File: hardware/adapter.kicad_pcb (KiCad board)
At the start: 2 copper layers, 51 parts

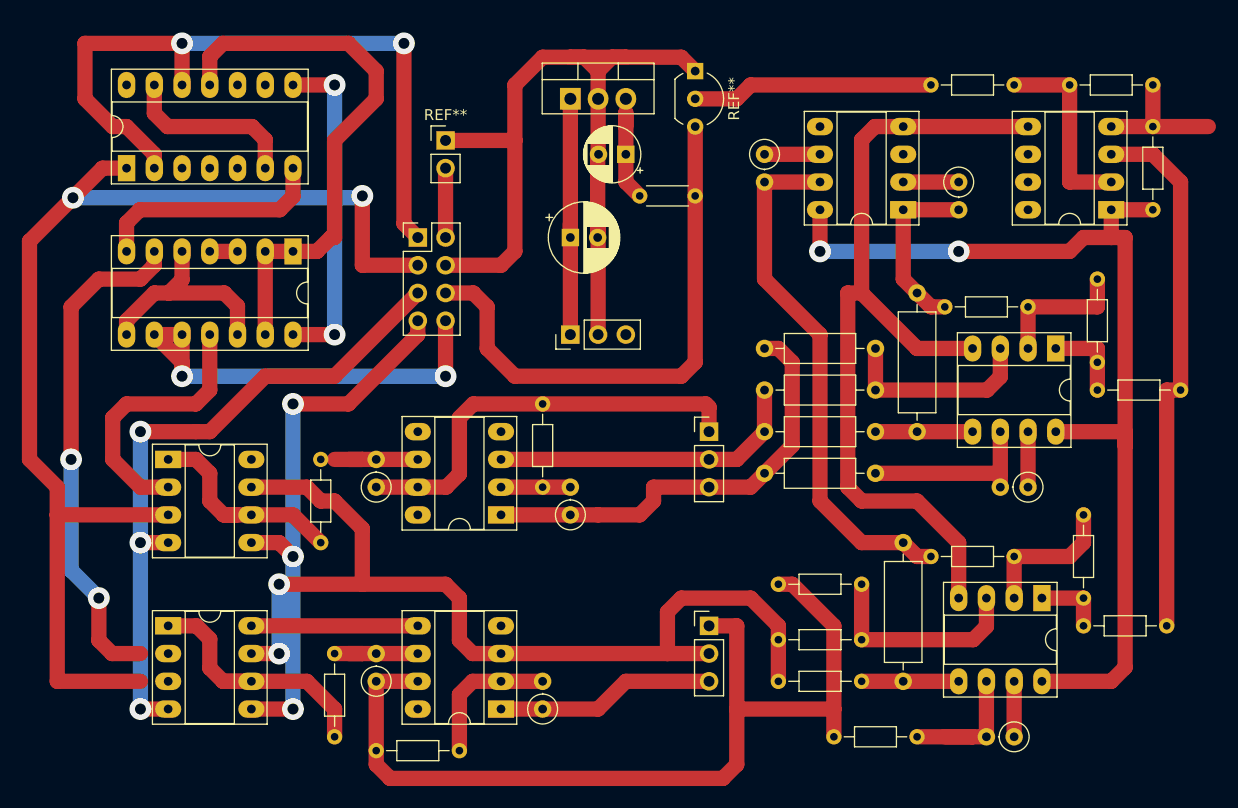
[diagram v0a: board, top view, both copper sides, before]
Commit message: Full hardware plate schema
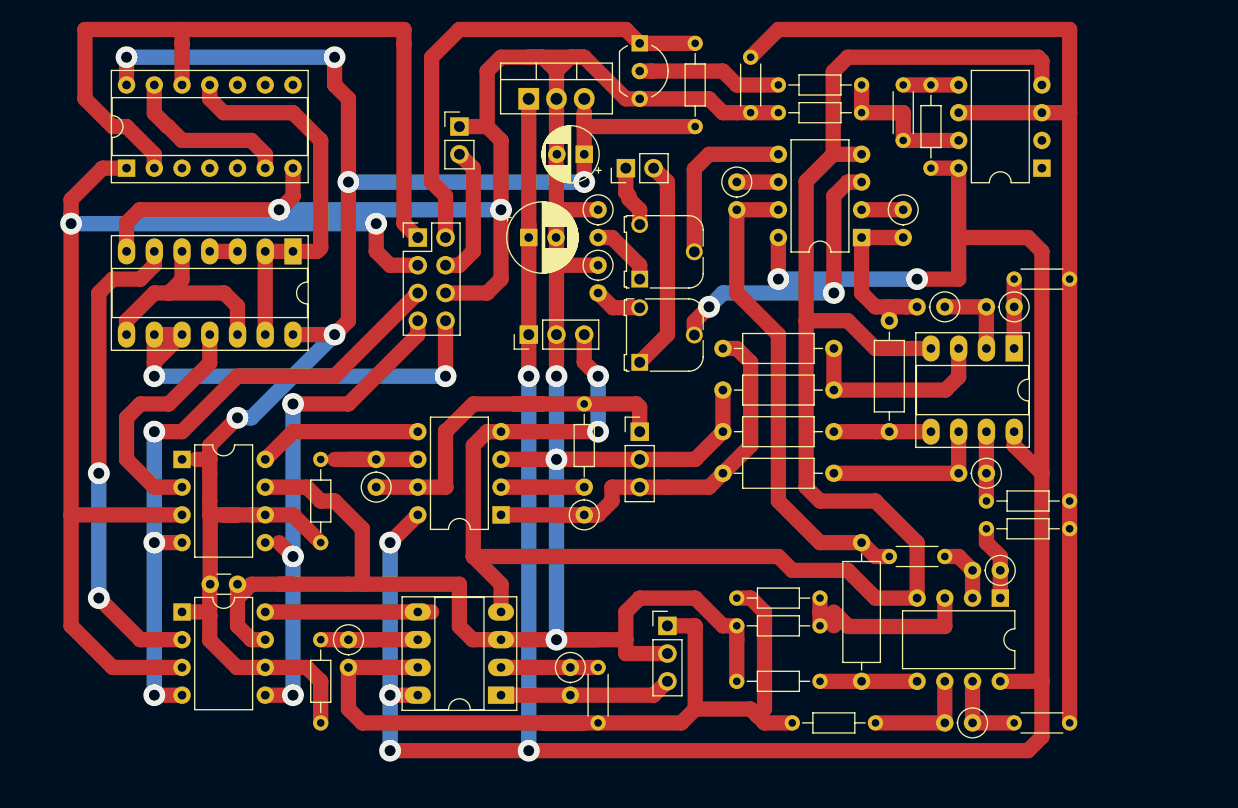
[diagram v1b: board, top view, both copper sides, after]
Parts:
- removed the REF** at (111.8, 27.9)
- removed the REF** at (118.1, 67.3)
- removed the REF** at (118.1, 49.5)
- removed the REF** at (68.6, 67.3)
- removed the REF** at (87.6, 78.7)
- removed the REF** at (151.1, 17.8)
- removed the REF** at (158.8, 21.6)
- removed the REF** at (153.7, 45.7)
- removed the REF** at (123.2, 53.3)
- removed the REF** at (123.2, 49.5)
- removed the REF** at (123.2, 45.7)
- removed the REF** at (154.9, 29.2)
- removed the REF** at (138.4, 61.0)
- removed the REF** at (152.4, 57.1)
- removed the REF** at (148.6, 64.8)
- removed the REF** at (139.7, 38.1)
- removed the REF** at (137.2, 36.8)
- removed the REF** at (153.7, 35.6)
- removed the REF** at (123.2, 24.1)
- removed the REF** at (141.0, 26.7)
- removed the REF** at (149.9, 41.9)
- removed the REF** at (135.9, 29.2)
- removed the REF** at (99.1, 57.1)
- removed the REF** at (68.6, 52.1)
- removed the REF** at (64.8, 25.4)
- removed the REF** at (105.4, 57.1)
- removed the REF** at (102.9, 74.9)
- added REF**: DIP-8_W7.62mm, Package_DIP:DIP-8_W7.62mm, F.Cu at (69.8, 52.1)
- added REF**: DIP-14_W7.62mm_Socket, Package_DIP:DIP-14_W7.62mm_Socket, F.Cu at (64.8, 25.4)
- added REF**: DIP-8_W7.62mm, Package_DIP:DIP-8_W7.62mm, F.Cu at (69.8, 66.0)
- added REF**: R_Axial_DIN0207_L6.3mm_D2.5mm_P2.54mm_Vertical, Resistor_THT:R_Axial_DIN0207_L6.3mm_D2.5mm_P2.54mm_Vertical, F.Cu at (108.0, 34.3)
- added REF**: R_Axial_DIN0207_L6.3mm_D2.5mm_P2.54mm_Vertical, Resistor_THT:R_Axial_DIN0207_L6.3mm_D2.5mm_P2.54mm_Vertical, F.Cu at (108.0, 29.2)
- added REF**: R_Axial_DIN0204_L3.6mm_D1.6mm_P7.62mm_Horizontal, Resistor_THT:R_Axial_DIN0204_L3.6mm_D1.6mm_P7.62mm_Horizontal, F.Cu at (116.8, 21.6)
- added REF**: PinHeader_1x02_P2.54mm_Vertical, Connector_PinHeader_2.54mm:PinHeader_1x02_P2.54mm_Vertical, F.Cu at (110.5, 25.4)
- added REF**: DIP-8_W7.62mm, Package_DIP:DIP-8_W7.62mm, F.Cu at (132.1, 31.8)
- added REF**: Potentiometer_Runtron_RM-065_Vertical, Potentiometer_THT:Potentiometer_Runtron_RM-065_Vertical, F.Cu at (111.8, 35.6)
- added REF**: R_Axial_DIN0204_L3.6mm_D1.6mm_P5.08mm_Horizontal, Resistor_THT:R_Axial_DIN0204_L3.6mm_D1.6mm_P5.08mm_Horizontal, F.Cu at (146.1, 76.2)
- added REF**: R_Axial_DIN0204_L3.6mm_D1.6mm_P7.62mm_Horizontal, Resistor_THT:R_Axial_DIN0204_L3.6mm_D1.6mm_P7.62mm_Horizontal, F.Cu at (143.5, 55.9)
- added REF**: DIP-8_W7.62mm, Package_DIP:DIP-8_W7.62mm, F.Cu at (148.6, 25.4)
- added REF**: DIP-8_W7.62mm, Package_DIP:DIP-8_W7.62mm, F.Cu at (144.8, 64.8)
- added REF**: DIP-8_W7.62mm, Package_DIP:DIP-8_W7.62mm, F.Cu at (99.1, 57.1)
- added REF**: R_Axial_DIN0204_L3.6mm_D1.6mm_P7.62mm_Horizontal, Resistor_THT:R_Axial_DIN0204_L3.6mm_D1.6mm_P7.62mm_Horizontal, F.Cu at (124.5, 17.8)
- added REF**: R_Axial_DIN0204_L3.6mm_D1.6mm_P5.08mm_Horizontal, Resistor_THT:R_Axial_DIN0204_L3.6mm_D1.6mm_P5.08mm_Horizontal, F.Cu at (135.9, 22.9)
- added REF**: R_Axial_DIN0207_L6.3mm_D2.5mm_P10.16mm_Horizontal, Resistor_THT:R_Axial_DIN0207_L6.3mm_D2.5mm_P10.16mm_Horizontal, F.Cu at (134.6, 49.5)
- added REF**: R_Axial_DIN0204_L3.6mm_D1.6mm_P5.08mm_Horizontal, Resistor_THT:R_Axial_DIN0204_L3.6mm_D1.6mm_P5.08mm_Horizontal, F.Cu at (146.1, 35.6)
- added REF**: Potentiometer_Runtron_RM-065_Vertical, Potentiometer_THT:Potentiometer_Runtron_RM-065_Vertical, F.Cu at (111.8, 43.2)
- added REF**: R_Axial_DIN0207_L6.3mm_D2.5mm_P2.54mm_Vertical, Resistor_THT:R_Axial_DIN0207_L6.3mm_D2.5mm_P2.54mm_Vertical, F.Cu at (144.8, 62.2)
- added REF**: R_Axial_DIN0207_L6.3mm_D2.5mm_P2.54mm_Vertical, Resistor_THT:R_Axial_DIN0207_L6.3mm_D2.5mm_P2.54mm_Vertical, F.Cu at (106.7, 57.1)
- added REF**: R_Axial_DIN0207_L6.3mm_D2.5mm_P2.54mm_Vertical, Resistor_THT:R_Axial_DIN0207_L6.3mm_D2.5mm_P2.54mm_Vertical, F.Cu at (105.4, 71.1)
- added REF**: PinHeader_1x03_P2.54mm_Vertical, Connector_PinHeader_2.54mm:PinHeader_1x03_P2.54mm_Vertical, F.Cu at (114.3, 67.3)
- added REF**: PinHeader_1x03_P2.54mm_Vertical, Connector_PinHeader_2.54mm:PinHeader_1x03_P2.54mm_Vertical, F.Cu at (111.8, 49.5)
- added REF**: R_Axial_DIN0204_L3.6mm_D1.6mm_P5.08mm_Horizontal, Resistor_THT:R_Axial_DIN0204_L3.6mm_D1.6mm_P5.08mm_Horizontal, F.Cu at (108.0, 76.2)
- added REF**: R_Axial_DIN0204_L3.6mm_D1.6mm_P5.08mm_Horizontal, Resistor_THT:R_Axial_DIN0204_L3.6mm_D1.6mm_P5.08mm_Horizontal, F.Cu at (134.6, 61.0)
- added REF**: R_Axial_DIN0207_L6.3mm_D2.5mm_P10.16mm_Horizontal, Resistor_THT:R_Axial_DIN0207_L6.3mm_D2.5mm_P10.16mm_Horizontal, F.Cu at (119.4, 53.3)
- added REF**: R_Axial_DIN0207_L6.3mm_D2.5mm_P10.16mm_Horizontal, Resistor_THT:R_Axial_DIN0207_L6.3mm_D2.5mm_P10.16mm_Horizontal, F.Cu at (119.4, 49.5)
- added REF**: R_Axial_DIN0207_L6.3mm_D2.5mm_P10.16mm_Horizontal, Resistor_THT:R_Axial_DIN0207_L6.3mm_D2.5mm_P10.16mm_Horizontal, F.Cu at (119.4, 45.7)
- added REF**: R_Axial_DIN0207_L6.3mm_D2.5mm_P2.54mm_Vertical, Resistor_THT:R_Axial_DIN0207_L6.3mm_D2.5mm_P2.54mm_Vertical, F.Cu at (146.1, 38.1)
- added REF**: R_Axial_DIN0207_L6.3mm_D2.5mm_P2.54mm_Vertical, Resistor_THT:R_Axial_DIN0207_L6.3mm_D2.5mm_P2.54mm_Vertical, F.Cu at (120.7, 26.7)
- added REF**: R_Axial_DIN0207_L6.3mm_D2.5mm_P2.54mm_Vertical, Resistor_THT:R_Axial_DIN0207_L6.3mm_D2.5mm_P2.54mm_Vertical, F.Cu at (135.9, 29.2)
- added REF**: DIP-8_W7.62mm_Socket_LongPads, Package_DIP:DIP-8_W7.62mm_Socket_LongPads, F.Cu at (146.1, 41.9)
- added REF**: R_Axial_DIN0207_L6.3mm_D2.5mm_P2.54mm_Vertical, Resistor_THT:R_Axial_DIN0207_L6.3mm_D2.5mm_P2.54mm_Vertical, F.Cu at (139.7, 38.1)
- added REF**: R_Axial_DIN0204_L3.6mm_D1.6mm_P7.62mm_Horizontal, Resistor_THT:R_Axial_DIN0204_L3.6mm_D1.6mm_P7.62mm_Horizontal, F.Cu at (138.4, 25.4)
- added REF**: C_Disc_D3.0mm_W1.6mm_P2.50mm, Capacitor_THT:C_Disc_D3.0mm_W1.6mm_P2.50mm, F.Cu at (74.9, 63.5)
- added REF**: R_Axial_DIN0204_L3.6mm_D1.6mm_P5.08mm_Horizontal, Resistor_THT:R_Axial_DIN0204_L3.6mm_D1.6mm_P5.08mm_Horizontal, F.Cu at (121.9, 20.3)
- moved REF** 14.2 mm to (124.5, 20.3)
- moved REF** 12.6 mm to (143.5, 58.4)
- moved REF** 5.68 mm to (111.8, 14.0)
- moved REF** 4.58 mm to (85.1, 68.6), turned to 270 degrees
- moved REF** 4.02 mm to (142.2, 76.2)
- moved REF** 4.02 mm to (143.5, 53.3)
- moved REF** 4.02 mm to (120.7, 64.8)
- moved REF** 4.02 mm to (120.7, 67.3)
- moved REF** 4.02 mm to (125.7, 76.2)
- moved REF** 3.81 mm to (119.4, 41.9)
- moved REF** 3.81 mm to (106.7, 54.6)
- moved REF** 3.81 mm to (101.6, 40.6)
- moved REF** 3.81 mm to (101.6, 31.8)
- moved REF** 3.81 mm to (101.6, 19.1)
- moved REF** 3.81 mm to (120.7, 72.4)
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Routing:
- net (no net): track 1596.7 -> 2018.2 mm, vias 20 -> 34

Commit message: Fix bug on hardware plate shemat
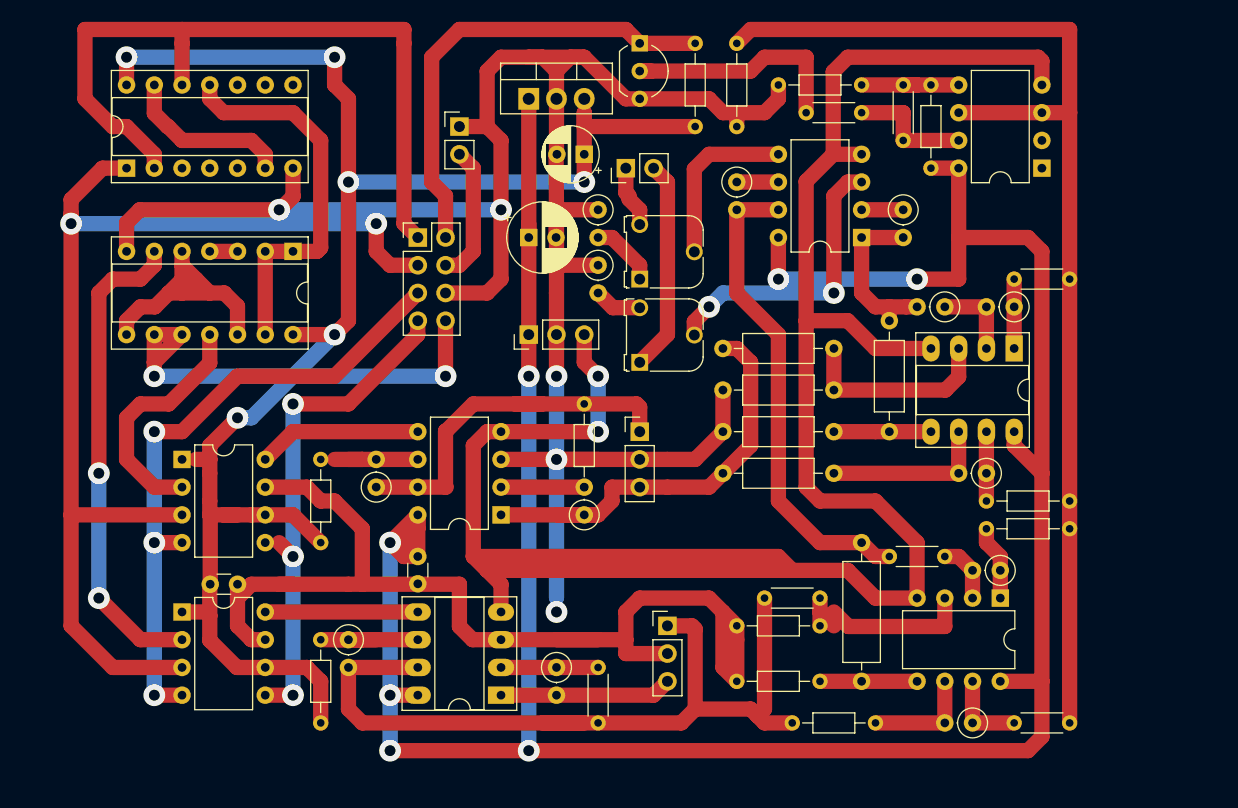
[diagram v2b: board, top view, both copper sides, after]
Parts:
- removed the REF** at (124.5, 20.3)
- removed the REF** at (80.0, 33.0)
- removed the REF** at (120.7, 64.8)
- added REF**: DIP-14_W7.62mm_Socket, Package_DIP:DIP-14_W7.62mm_Socket, F.Cu at (80.0, 33.0)
- added REF**: C_Disc_D3.0mm_W1.6mm_P2.50mm, Capacitor_THT:C_Disc_D3.0mm_W1.6mm_P2.50mm, F.Cu at (91.4, 61.0)
- added REF**: R_Axial_DIN0204_L3.6mm_D1.6mm_P7.62mm_Horizontal, Resistor_THT:R_Axial_DIN0204_L3.6mm_D1.6mm_P7.62mm_Horizontal, F.Cu at (132.1, 17.8)
- added REF**: R_Axial_DIN0204_L3.6mm_D1.6mm_P5.08mm_Horizontal, Resistor_THT:R_Axial_DIN0204_L3.6mm_D1.6mm_P5.08mm_Horizontal, F.Cu at (123.2, 64.8)
- moved REF** 10.2 mm to (132.1, 20.3), turned to 180 degrees
- moved REF** 5.39 mm to (120.7, 21.6), turned to 90 degrees
- moved REF** 1.27 mm to (104.1, 71.1)
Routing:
- net (no net): track 2018.2 -> 2077.7 mm

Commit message: Add capacitor
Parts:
- added REF**: R_Axial_DIN0204_L3.6mm_D1.6mm_P7.62mm_Horizontal, Resistor_THT:R_Axial_DIN0204_L3.6mm_D1.6mm_P7.62mm_Horizontal, F.Cu at (62.2, 27.9)
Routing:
- net (no net): track 2077.7 -> 2091.5 mm
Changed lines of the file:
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@@
   (general
     (thickness 1.6)
-    (drawings 3)
-    (tracks 464)
+    (drawings 4)
+    (tracks 466)
     (zones 0)
-    (modules 62)
+    (modules 63)
     (nets 1)
   )
@@
       (outputformat 1)
       (mirror false)
-      (drillshape 1)
+      (drillshape 0)
       (scaleselection 1)
       (outputdirectory ""))
@@
     (uvia_drill 0.1)
   )
+  (module Resistor_THT:R_Axial_DIN0204_L3.6mm_D1.6mm_P7.62mm_Horizontal (layer F.Cu)
+    (at 62.23 27.94 90)
+    (descr "Resistor, Axial_DIN0204 series, Axial, Horizontal, pin pitch=7.62mm, 0.167W, length*diameter=3.6*1.6mm^2, http://cdn-reichelt.de/documents/datenblatt/B400/1_4W%23YAG.pdf")
+    (tags "Resistor Axial_DIN0204 series Axial Horizontal pin pitch 7.62mm 0.167W length 3.6mm diameter 1.6mm")
+    (fp_text reference REF** (at 3.81 -1.92 90) (layer F.SilkS) hide
+      (effects (font (size 1 1) (thickness 0.15)))
+    )
+    (fp_text value R_Axial_DIN0204_L3.6mm_D1.6mm_P7.62mm_Horizontal (at 3.81 1.92 90) (layer F.Fab) hide
+      (effects (font (size 1 1) (thickness 0.15)))
+    )
+    (fp_line (start 2.01 -0.8) (end 2.01 0.8) (layer F.Fab) (width 0.1))
+    (fp_line (start 2.01 0.8) (end 5.61 0.8) (layer F.Fab) (width 0.1))
+    (fp_line (start 5.61 0.8) (end 5.61 -0.8) (layer F.Fab) (width 0.1))
+    (fp_line (start 5.61 -0.8) (end 2.01 -0.8) (layer F.Fab) (width 0.1))
+    (fp_line (start 0 0) (end 2.01 0) (layer F.Fab) (width 0.1))
+    (fp_line (start 7.62 0) (end 5.61 0) (layer F.Fab) (width 0.1))
+    (fp_line (start 1.89 -0.92) (end 1.89 0.92) (layer F.SilkS) (width 0.12))
+    (fp_line (start 1.89 0.92) (end 5.73 0.92) (layer F.SilkS) (width 0.12))
+    (fp_line (start 5.73 0.92) (end 5.73 -0.92) (layer F.SilkS) (width 0.12))
+    (fp_line (start 5.73 -0.92) (end 1.89 -0.92) (layer F.SilkS) (width 0.12))
+    (fp_line (start 0.94 0) (end 1.89 0) (layer F.SilkS) (width 0.12))
+    (fp_line (start 6.68 0) (end 5.73 0) (layer F.SilkS) (width 0.12))
+    (fp_line (start -0.95 -1.05) (end -0.95 1.05) (layer F.CrtYd) (width 0.05))
+    (fp_line (start -0.95 1.05) (end 8.57 1.05) (layer F.CrtYd) (width 0.05))
+    (fp_line (start 8.57 1.05) (end 8.57 -1.05) (layer F.CrtYd) (width 0.05))
+    (fp_line (start 8.57 -1.05) (end -0.95 -1.05) (layer F.CrtYd) (width 0.05))
+    (fp_text user 4.7k (at 3.81 0 90) (layer F.Fab)
+      (effects (font (size 0.72 0.72) (thickness 0.108)))
+    )
+    (pad 1 thru_hole circle (at 0 0 90) (size 1.4 1.4) (drill 0.7) (layers *.Cu *.Mask))
+    (pad 2 thru_hole oval (at 7.62 0 90) (size 1.4 1.4) (drill 0.7) (layers *.Cu *.Mask))
+    (model ${KISYS3DMOD}/Resistor_THT.3dshapes/R_Axial_DIN0204_L3.6mm_D1.6mm_P7.62mm_Horizontal.wrl
+      (at (xyz 0 0 0))
+      (scale (xyz 1 1 1))
+      (rotate (xyz 0 0 0))
+    )
+  )
   (module Package_DIP:DIP-14_W7.62mm_Socket (layer F.Cu)
     (at 80.01 33.02 270)
@@
     )
   )
+  (gr_poly (pts (xy 87.63 26.67) (xy 85.09 26.67) (xy 83.82 15.24) (xy 87.63 15.24)) (layer Cmts.User) (width 0.1))
   (gr_poly (pts (xy 148.59 33.02) (xy 140.97 33.02) (xy 140.97 27.94) (xy 148.59 27.94)) (layer Cmts.User) (width 0.1))
   (gr_poly (pts (xy 110.49 68.58) (xy 102.87 68.58) (xy 102.87 64.77) (xy 111.76 64.77)) (layer Cmts.User) (width 0.1))
@@
   (via (at 62.23 53.34) (size 2) (drill 1) (layers F.Cu B.Cu) (net 0))
   (via (at 62.23 64.77) (size 2) (drill 1) (layers F.Cu B.Cu) (net 0))
-  (segment (start 64.77 25.4) (end 62.57 25.4) (width 1.4) (layer F.Cu) (net 0))
   (segment (start 69.85 13.97) (end 69.85 17.78) (width 1.4) (layer F.Cu) (net 0))
   (segment (start 80.01 28) (end 80.01 27.94) (width 1.4) (layer F.Cu) (net 0))
   (segment (start 65.98 29.21) (end 78.8 29.21) (width 1.4) (layer F.Cu) (net 0))
   (segment (start 78.8 29.21) (end 80.01 28) (width 1.4) (layer F.Cu) (net 0))
-  (segment (start 64.77 30.42) (end 65.98 29.21) (width 1.4) (layer F.Cu) (net 0))
   (segment (start 64.77 33.02) (end 64.77 30.42) (width 1.4) (layer F.Cu) (net 0))
   (segment (start 83.82 40.64) (end 80.01 40.64) (width 1.4) (layer F.Cu) (net 0))
@@
   (segment (start 85.09 39.37) (end 85.09 26.67) (width 1.4) (layer F.Cu) (net 0))
   (segment (start 69.85 12.7) (end 69.85 13.97) (width 1.4) (layer F.Cu) (net 0))
-  (segment (start 60.96 12.7) (end 69.85 12.7) (width 1.4) (layer F.Cu) (net 0))
-  (segment (start 60.96 19.05) (end 60.96 12.7) (width 1.4) (layer F.Cu) (net 0))
-  (segment (start 63.5 21.59) (end 60.96 19.05) (width 1.4) (layer F.Cu) (net 0))
-  (segment (start 67.31 24.13) (end 64.77 21.59) (width 1.4) (layer F.Cu) (net 0))
-  (segment (start 64.77 21.59) (end 63.5 21.59) (width 1.4) (layer F.Cu) (net 0))
   (segment (start 67.31 25.4) (end 67.31 24.13) (width 1.4) (layer F.Cu) (net 0))
   (segment (start 69.85 12.7) (end 90.17 12.7) (width 1.4) (layer F.Cu) (net 0))
@@
   (segment (start 63.5 35.56) (end 66.04 35.56) (width 1.4) (layer F.Cu) (net 0))
   (segment (start 62.23 36.83) (end 63.5 35.56) (width 1.4) (layer F.Cu) (net 0))
-  (segment (start 59.69 28.28) (end 62.57 25.4) (width 1.4) (layer F.Cu) (net 0))
-  (segment (start 59.69 30.48) (end 59.69 28.28) (width 1.4) (layer F.Cu) (net 0))
   (segment (start 59.69 30.48) (end 87.63 30.48) (width 1.4) (layer B.Cu) (net 0))
   (segment (start 101.6 78.74) (end 147.32 78.74) (width 1.4) (layer F.Cu) (net 0))
@@
   (segment (start 69.85 34.29) (end 71.12 35.56) (width 1.4) (layer F.Cu) (net 0))
   (segment (start 71.12 35.56) (end 72.39 36.83) (width 1.4) (layer F.Cu) (net 0))
+  (segment (start 59.69 12.7) (end 69.85 12.7) (width 1.4) (layer F.Cu) (net 0))
+  (segment (start 64.77 25.4) (end 59.69 25.4) (width 1.4) (layer F.Cu) (net 0))
+  (segment (start 59.69 25.4) (end 59.69 30.48) (width 1.4) (layer F.Cu) (net 0))
+  (segment (start 59.69 12.7) (end 59.69 22.86) (width 1.4) (layer F.Cu) (net 0))
+  (segment (start 59.69 22.86) (end 66.04 22.86) (width 1.4) (layer F.Cu) (net 0))
+  (segment (start 66.04 22.86) (end 67.31 24.13) (width 1.4) (layer F.Cu) (net 0))
+  (segment (start 62.23 20.32) (end 64.77 17.78) (width 1.4) (layer F.Cu) (net 0))
+  (segment (start 63.5 27.94) (end 64.77 29.21) (width 1.4) (layer F.Cu) (net 0))
+  (segment (start 64.77 29.21) (end 65.98 29.21) (width 1.4) (layer F.Cu) (net 0))
+  (segment (start 62.23 27.94) (end 63.5 27.94) (width 1.4) (layer F.Cu) (net 0))
+  (segment (start 64.77 30.42) (end 64.77 29.21) (width 1.4) (layer F.Cu) (net 0))
 )
